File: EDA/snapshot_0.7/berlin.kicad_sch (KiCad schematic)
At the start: 444 parts, among them J201 TYPE-C-31-M12_13, J202 Conn_ARM_JTAG_SWD_10, J203 LCDCON, Q701 DTC123J, SW1,1 Rotary_Encoder_Switch_Chassis, SW1,10 MXSwitch, SW1,11 MXSwitch, SW1,12 MXSwitch, SW1,13 MXSwitch, SW1,14 MXSwitch, SW1,15 MXSwitch, SW1,16 Rotary_Encoder_Switch_Chassis, SW1,2 MXSwitch, SW1,3 MXSwitch, SW1,4 MXSwitch, SW1,5 MXSwitch, SW1,6 MXSwitch, SW1,7 MXSwitch, SW1,8 MXSwitch, SW1,9 MXSwitch, SW2,1 MXSwitch, SW2,10 MXSwitch, SW2,11 MXSwitch, SW2,12 MXSwitch, SW2,13 MXSwitch, SW2,14 MXSwitch, SW2,15 MXSwitch, SW2,16 MXSwitch, SW2,17 MXSwitch, SW2,18 MXSwitch, SW2,19 MXSwitch, SW2,2 MXSwitch, SW2,3 MXSwitch, SW2,4 MXSwitch, SW2,5 MXSwitch, SW2,6 MXSwitch, SW2,7 MXSwitch, SW2,8 MXSwitch, SW2,9 MXSwitch, SW201 SW_Push, SW202 SW_Push, SW3,1 MXSwitch, SW3,10 MXSwitch, SW3,11 MXSwitch, SW3,12 MXSwitch, SW3,13 MXSwitch, SW3,14 MXSwitch, SW3,15 MXSwitch, SW3,16 MXSwitch, SW3,17 MXSwitch, SW3,18 MXSwitch, SW3,19 MXSwitch, SW3,2 MXSwitch, SW3,3 MXSwitch, SW3,4 MXSwitch, SW3,5 MXSwitch, SW3,6 MXSwitch, SW3,7 MXSwitch, SW3,8 MXSwitch, SW3,9 MXSwitch, SW4,1 MXSwitch, SW4,10 MXSwitch, SW4,11 MXSwitch, SW4,12 MXSwitch, SW4,13 MXSwitch, SW4,14 MXSwitch, SW4,15 MXSwitch, SW4,16 MXSwitch, SW4,17 MXSwitch, SW4,18 MXSwitch, SW4,19 MXSwitch, SW4,2 MXSwitch, SW4,3 MXSwitch, SW4,4 MXSwitch, SW4,5 MXSwitch, SW4,6 MXSwitch, SW4,7 MXSwitch, SW4,8 MXSwitch, SW4,9 MXSwitch, SW5,1 MXSwitch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

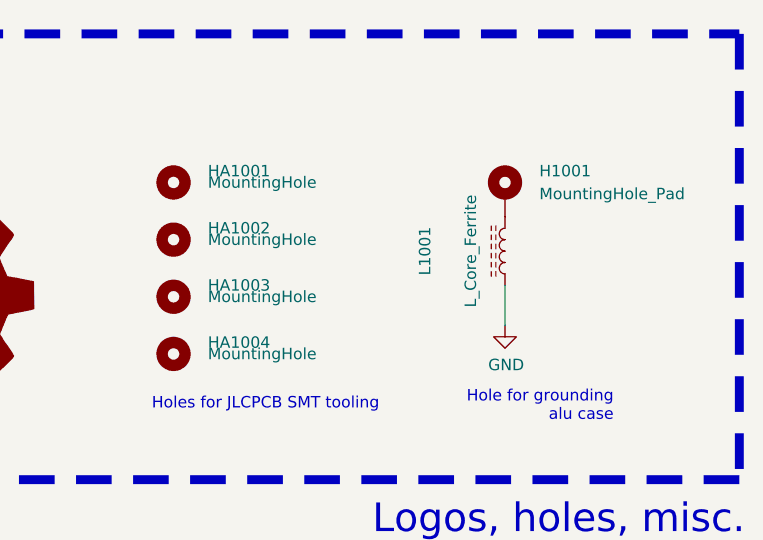
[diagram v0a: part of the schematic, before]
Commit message: 0.7 add mounting holes & branding
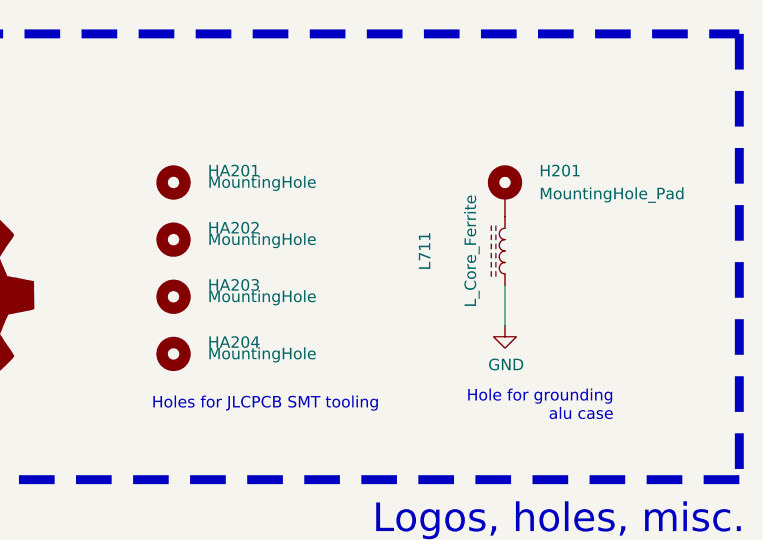
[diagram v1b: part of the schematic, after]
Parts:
- renumbered H1001 to H201, HA1001 to HA201, HA1002 to HA202, HA1003 to HA203, HA1004 to HA204, L1001 to L711, LOGO1001 to LOGO201
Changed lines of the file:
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@@
   (symbol (lib_id "Mechanical:MountingHole") (at 1109.98 50.8 0) (unit 1)
     (in_bom yes) (on_board yes)
-    (property "Reference" "HA1004" (id 0) (at 1113.79 49.53 0)
+    (property "Reference" "HA204" (id 0) (at 1113.79 49.53 0)
       (effects (font (size 1.27 1.27)) (justify left))
     )
@@
   (symbol (lib_id "Mechanical:MountingHole") (at 1109.98 44.45 0) (unit 1)
     (in_bom yes) (on_board yes)
-    (property "Reference" "HA1003" (id 0) (at 1113.79 43.18 0)
+    (property "Reference" "HA203" (id 0) (at 1113.79 43.18 0)
       (effects (font (size 1.27 1.27)) (justify left))
     )
@@
   (symbol (lib_id "Graphic:Logo_Open_Hardware_Large") (at 1083.31 44.45 0) (unit 1)
     (in_bom yes) (on_board yes)
-    (property "Reference" "LOGO1001" (id 0) (at 1083.31 31.75 0)
+    (property "Reference" "LOGO201" (id 0) (at 1083.31 31.75 0)
       (effects (font (size 1.27 1.27)) hide)
     )
@@
   (symbol (lib_id "Mechanical:MountingHole") (at 1109.98 38.1 0) (unit 1)
     (in_bom yes) (on_board yes)
-    (property "Reference" "HA1002" (id 0) (at 1113.79 36.83 0)
+    (property "Reference" "HA202" (id 0) (at 1113.79 36.83 0)
       (effects (font (size 1.27 1.27)) (justify left))
     )
@@
   (symbol (lib_id "Mechanical:MountingHole_Pad") (at 1146.81 33.02 0) (unit 1)
     (in_bom yes) (on_board yes)
-    (property "Reference" "H1001" (id 0) (at 1150.62 30.48 0)
+    (property "Reference" "H201" (id 0) (at 1150.62 30.48 0)
       (effects (font (size 1.27 1.27)) (justify left))
     )
@@
   (symbol (lib_id "Device:L_Core_Ferrite") (at 1146.81 39.37 180) (unit 1)
     (in_bom yes) (on_board yes)
-    (property "Reference" "L1001" (id 0) (at 1137.92 39.37 90))
+    (property "Reference" "L711" (id 0) (at 1137.92 39.37 90))
     (property "Value" "L_Core_Ferrite" (id 1) (at 1143 39.37 90))
     (property "Footprint" "Inductor_SMD:L_0805_2012Metric_Pad1.15x1.40mm_HandSolder" (id 2) (at 1146.81 39.37 0)
@@
   (symbol (lib_id "Mechanical:MountingHole") (at 1109.98 31.75 0) (unit 1)
     (in_bom yes) (on_board yes)
-    (property "Reference" "HA1001" (id 0) (at 1113.79 30.48 0)
+    (property "Reference" "HA201" (id 0) (at 1113.79 30.48 0)
       (effects (font (size 1.27 1.27)) (justify left))
     )
@@
     )
     (path "/8061ecd2-b448-4175-bfb2-5bc2273e1626"
-      (reference "H1001") (unit 1) (value "MountingHole_Pad") (footprint "MountingHole:MountingHole_3.5mm_Pad_Via")
+      (reference "H201") (unit 1) (value "MountingHole_Pad") (footprint "MountingHole:MountingHole_3.5mm_Pad_Via")
     )
     (path "/c397abdf-dc25-4bc0-8ce4-aae95d0b72ab"
-      (reference "HA1001") (unit 1) (value "MountingHole") (footprint "acheronMountingHoles:ToolingHole_1.152mm_(for_JLCPCB_SMT)")
+      (reference "HA201") (unit 1) (value "MountingHole") (footprint "acheronMountingHoles:ToolingHole_1.152mm_(for_JLCPCB_SMT)")
     )
     (path "/63d70738-7b0d-413e-b3fc-00425503fbad"
-      (reference "HA1002") (unit 1) (value "MountingHole") (footprint "acheronMountingHoles:ToolingHole_1.152mm_(for_JLCPCB_SMT)")
+      (reference "HA202") (unit 1) (value "MountingHole") (footprint "acheronMountingHoles:ToolingHole_1.152mm_(for_JLCPCB_SMT)")
     )
     (path "/56012636-1ba8-4746-a9a5-ab167d70106d"
-      (reference "HA1003") (unit 1) (value "MountingHole") (footprint "acheronMountingHoles:ToolingHole_1.152mm_(for_JLCPCB_SMT)")
+      (reference "HA203") (unit 1) (value "MountingHole") (footprint "acheronMountingHoles:ToolingHole_1.152mm_(for_JLCPCB_SMT)")
     )
     (path "/13cfc6d7-0e8f-483c-9179-ea79c669bd75"
-      (reference "HA1004") (unit 1) (value "MountingHole") (footprint "acheronMountingHoles:ToolingHole_1.152mm_(for_JLCPCB_SMT)")
+      (reference "HA204") (unit 1) (value "MountingHole") (footprint "acheronMountingHoles:ToolingHole_1.152mm_(for_JLCPCB_SMT)")
     )
     (path "/199c68db-db42-409d-a53e-b530f9f4274e"
@@
     )
     (path "/87bed887-4561-4d19-8e44-a1cfedaafa26"
-      (reference "L1001") (unit 1) (value "L_Core_Ferrite") (footprint "Inductor_SMD:L_0805_2012Metric_Pad1.15x1.40mm_HandSolder")
+      (reference "L711") (unit 1) (value "L_Core_Ferrite") (footprint "Inductor_SMD:L_0805_2012Metric_Pad1.15x1.40mm_HandSolder")
     )
     (path "/ec436172-43c1-41cf-b093-6e150e0e1eb6"
@@
     )
     (path "/5860b9d7-2154-425c-b22c-6d5472216d65"
-      (reference "LOGO1001") (unit 1) (value "Logo_Open_Hardware_Large") (footprint "Symbol:OSHW-Logo_11.4x12mm_SilkScreen")
+      (reference "LOGO201") (unit 1) (value "Logo_Open_Hardware_Large") (footprint "Symbol:OSHW-Logo_11.4x12mm_SilkScreen")
     )
     (path "/cd6c4e0c-0e3e-425e-b923-c3646427d83c"

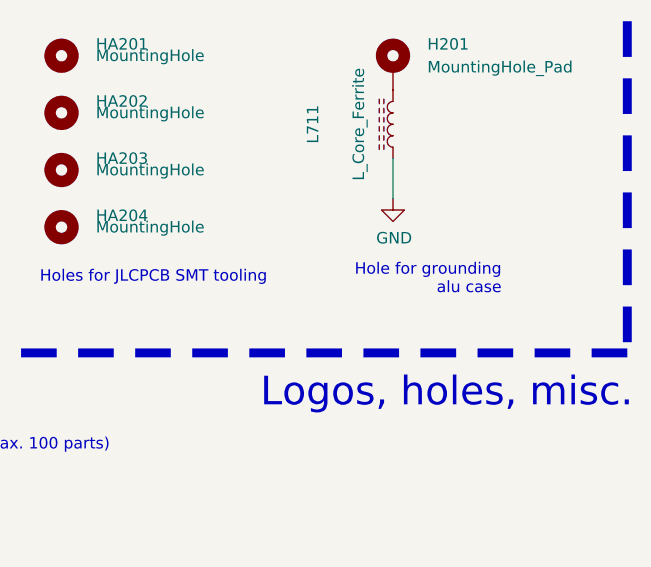
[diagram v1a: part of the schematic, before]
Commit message: Add two more switches for fun
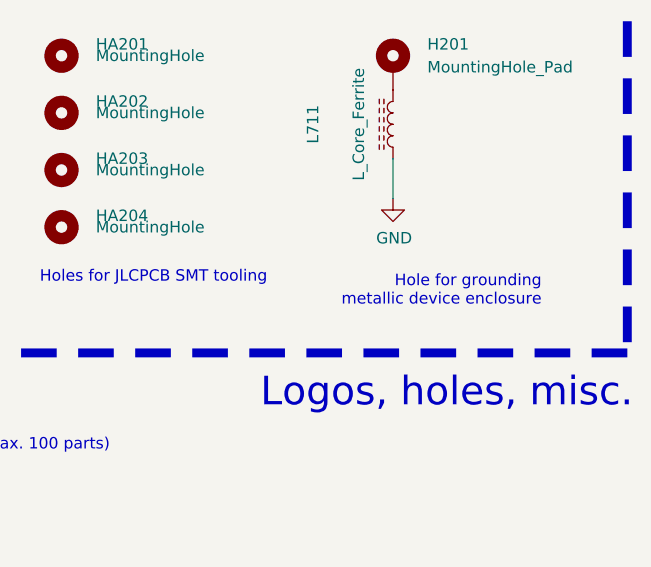
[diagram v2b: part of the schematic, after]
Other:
- note added: "Hole for grounding metallic device enclosure"
- note removed: "Hole for grounding alu case"
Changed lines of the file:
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@@
     (effects (font (size 1.27 1.27)) (justify left bottom))
   )
-  (text "Hole for grounding\nalu case" (at 1158.875 58.42 180)
+  (text "Hole for grounding\nmetallic device enclosure\n" (at 1163.32 59.69 180)
     (effects (font (size 1.27 1.27)) (justify right bottom))
   )

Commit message: append last 2 commits to comply with standards
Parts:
- added D125, D126, D127, D128, D129: 1N4148, acheronComponents:D_SOD-123, symbol Diode:1N4148
- added JMP6,14, JMP6,16: SolderJumper_2_Bridged, symbol Jumper:SolderJumper_2_Bridged
- added LED6,14, LED6,16: SK6812MINI-E, acheron_Components:SK6812MINI_3535_6028_3.2x2.8mm_Round, symbol 2022-03-27_15-42-261:SK6812MINI-E
- added SW6,14, SW6,16, SW7,4, SW7,5, SW7,7: MXSwitch, acheron_MX:MX100, symbol Boston-keyboard-rescue:MXSwitch-Acheron
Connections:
- net +5V: now also LED6,14.1 (5V), LED6,16.1 (5V)
- net Col14: now also SW6,14.1 (Col)
- net Col16: now also SW6,16.1 (Col)
- net Col4: now also SW7,4.1 (Col)
- net Col5: now also SW7,5.1 (Col)
- net Col7: now also SW7,7.1 (Col)
- net GND: now also LED6,13.4 (DIN), LED6,15.4 (DIN), JMP6,14.1 (A), JMP6,16.1 (A), LED6,14.2 (DOUT), LED6,14.3 (GND), LED6,16.2 (DOUT), LED6,16.3 (GND)
- net Row6: now also D128.1 (K), D129.1 (K)
- net Row7: now also D125.1 (K), D126.1 (K), D127.1 (K)
- net at LED6,17.2 (DOUT): now also JMP6,16.2 (B), LED6,16.4 (DIN); no longer LED6,15.4 (DIN)
- net at LED6,15.2 (DOUT): now also JMP6,14.2 (B), LED6,14.4 (DIN); no longer LED6,13.4 (DIN)
- new net: D125.2 (A), SW7,4.2 (Row)
- new net: D127.2 (A), SW7,7.2 (Row)
- new net: D126.2 (A), SW7,5.2 (Row)
- new net: D128.2 (A), SW6,14.2 (Row)
- new net: D129.2 (A), SW6,16.2 (Row)

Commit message: Fix schematic: The selected rotary encoder is weird. This is the actual design we are building.
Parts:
- SW1,1: symbol acheronSymbols:Rotary_Encoder_Switch_Chassis -> RotaryEncodersCustom:Rotary_cursed
